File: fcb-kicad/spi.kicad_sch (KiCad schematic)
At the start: 0 parts

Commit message: hierarchic schemas, paljon muuta kivaa
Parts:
- added C10, C9: 100n, Capacitor_SMD:C_0603_1608Metric, symbol Device:C_Small
- added U3: DL-RTS4432, 000_sjt:DL-RTS4432_board, symbol 000_sjt:DL-RTS4432
- added U4, U7: LSM6DS3, Package_LGA:LGA-14_3x2.5mm_P0.5mm_LayoutBorder3x4y, symbol Sensor_Motion:LSM6DS3
- added U6: W25Q128JVS, Package_SO:SOIC-8_5.23x5.23mm_P1.27mm, symbol Memory_Flash:W25Q128JVS
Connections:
- new net: C10.1, U7.8 (VDD)
- new net: C9.1, U7.5 (VDDIO)
- new net +3V3: C10.2, C9.2
- new net GND: U7.2 (SDX), U7.3 (SCX), U7.6 (GND), U7.7 (GND)
- new net IMU_CS: U7.12 (CS)
- new net IMU_INT1: U7.4 (INT1)
- new net IMU_INT2: U7.9 (INT2)
- new net IMU_SDI: U7.14 (SDA)
- new net IMU_SDO: U7.1 (SDO/SA0)
- new net IMU_SPC: U7.13 (SCL)
- new net RAD_CS_N: U3.13 (nSEL)
- new net RAD_GPIO_0: U3.6 (GPIO_0)
- new net RAD_IRQ_N: U3.14 (nIRQ)
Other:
- note added: "CS: (1: SPI idle mode, 0: spi communication mode)"
- note added: "Datasheet has separate VDD and VDDIO VDDIO = Power supply for I/O pins Currently both connected to 3V3 VDD: 1.71-3.6 (V) VDDIO: 1.62-VDD + 0.1 (V)"
- note added: "IMU CIRCUIT"
- note added: "INT1: Programmable interrupt 1"
- note added: "SDI: SPI serial data input"
- note added: "SDO: SPI 4-wire interface serial data output"
- note added: "SDX and SCX can be alternatively connected to VDDIO"
- note added: "SPC: SPI serial port clock"
- company: (none) -> University of Oulu

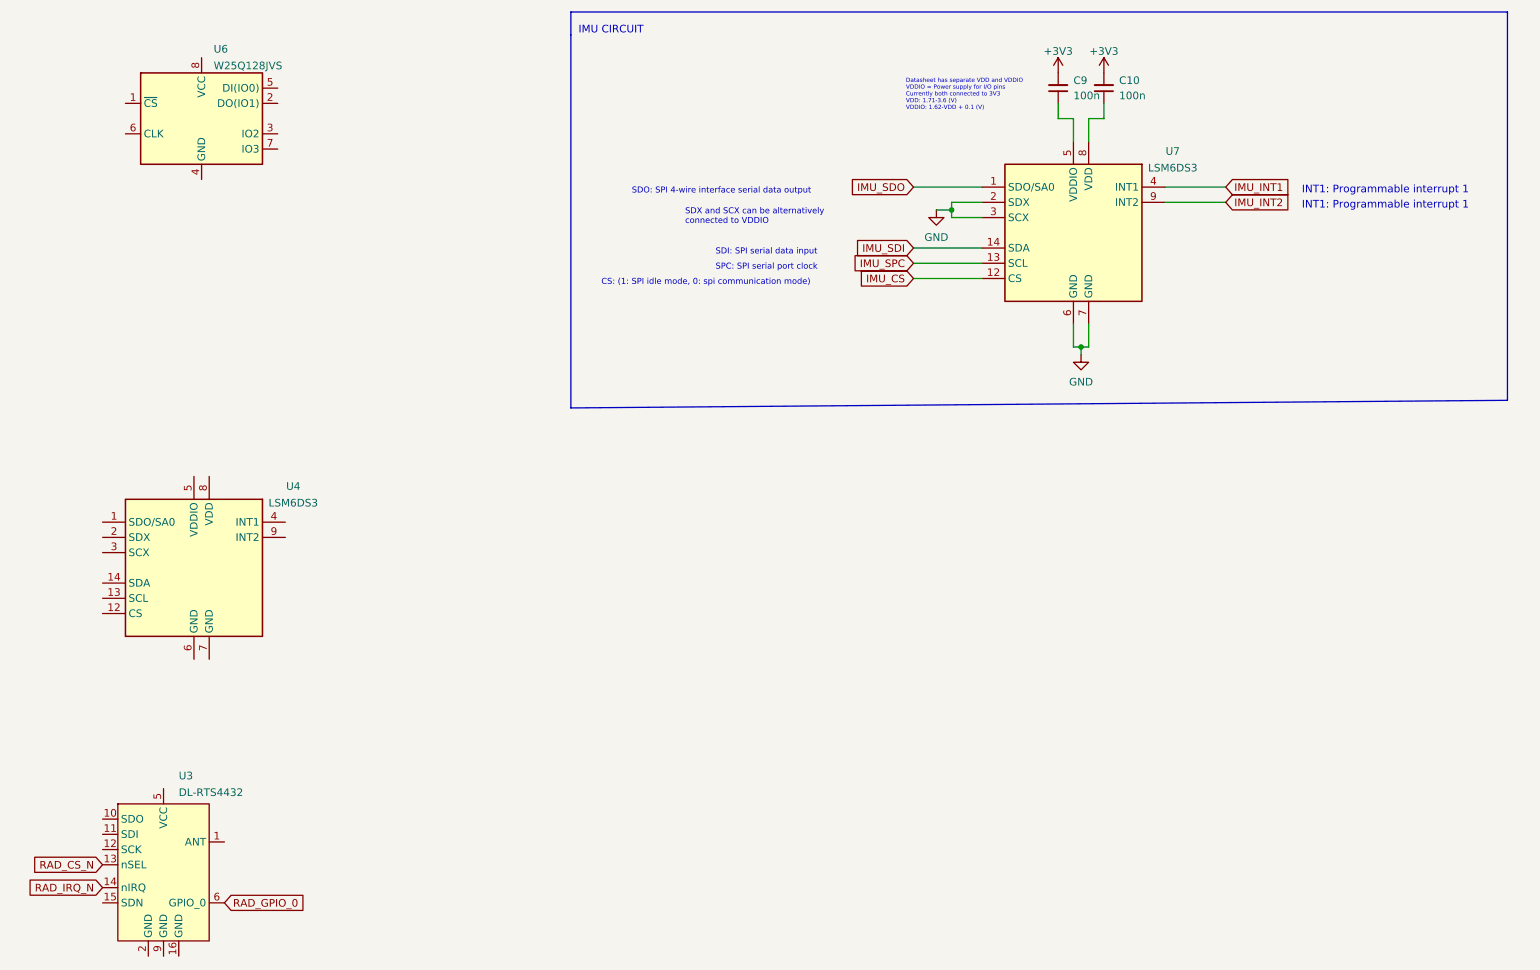
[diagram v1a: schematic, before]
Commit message: 4in1 connector library part, SPI CS pullups, migrate magnetometer cirtuit
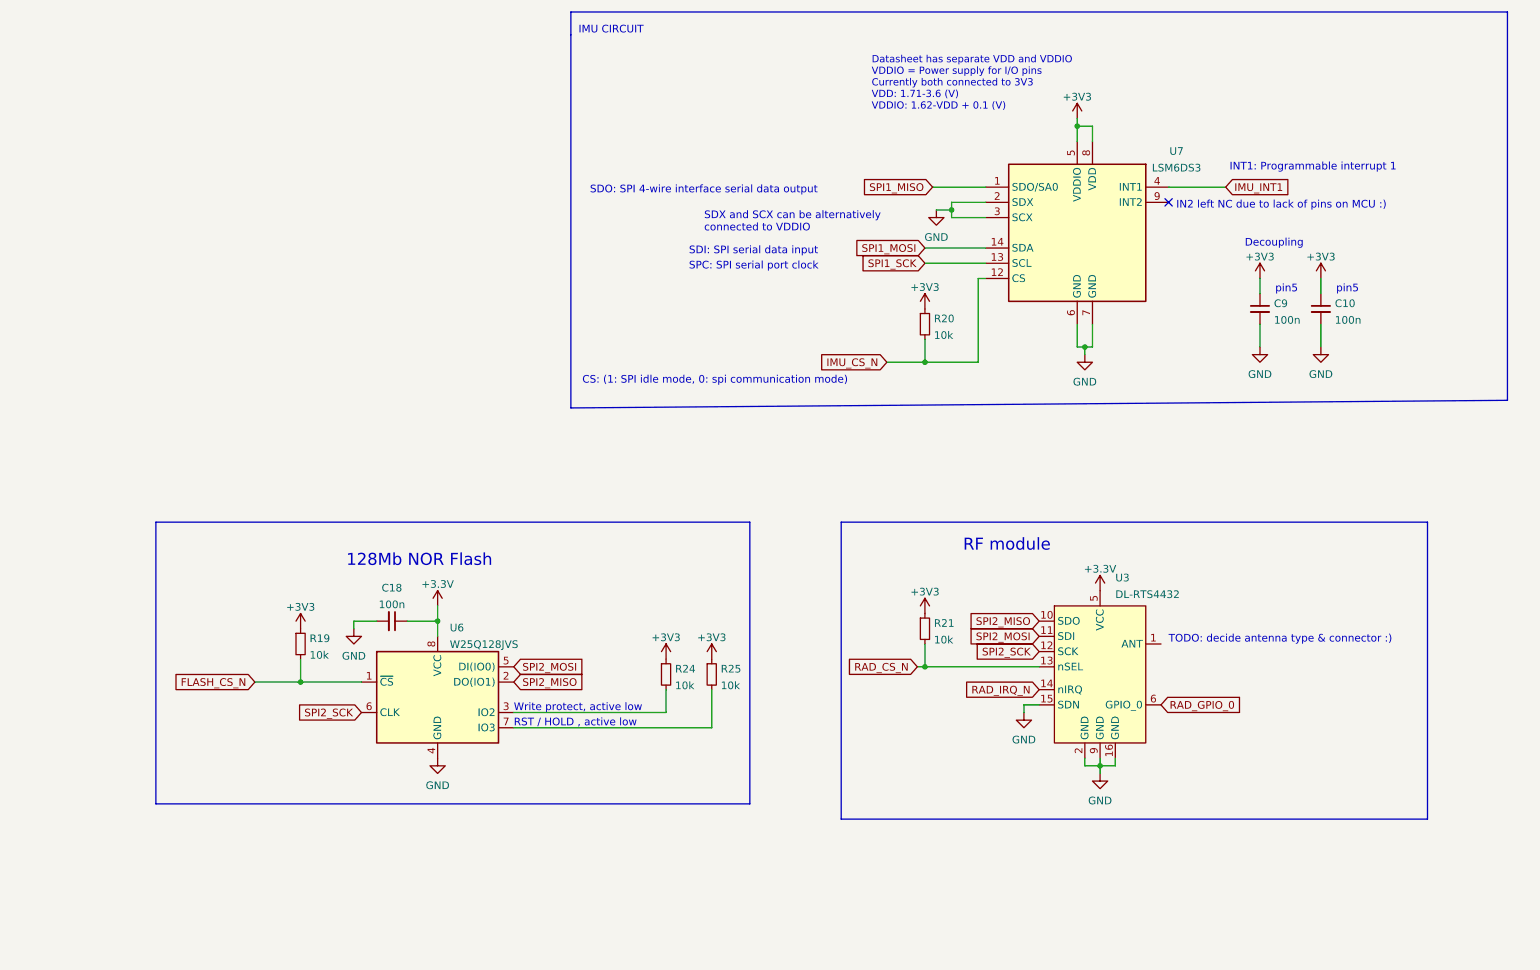
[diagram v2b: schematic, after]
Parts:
- removed U4: LSM6DS3, Package_LGA:LGA-14_3x2.5mm_P0.5mm_LayoutBorder3x4y, symbol Sensor_Motion:LSM6DS3
- added C18: 100n, Capacitor_SMD:C_0603_1608Metric, symbol Device:C_Small
- added R19, R20, R21, R24, R25: 10k, symbol Device:R_Small
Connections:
- net +3V3: now also C10.1, C9.1, U3.5 (VCC), U6.8 (VCC), U7.5 (VDDIO), U7.8 (VDD), C18.1, R19.1, R20.1, R21.1, R24.1, R25.1; no longer C10.2, C9.2
- net GND: now also C10.2, C9.2, U3.15 (SDN), U3.16 (GND), U3.2 (GND), U3.9 (GND), U6.4 (GND), C18.2
- net RAD_CS_N: now also R21.2
- net FLASH_CS_N: now reaches U6.1 (~{CS})
- net FLASH_CS_N: now also R19.2
- net SPI2_MISO: now reaches U6.2 (DO(IO1))
- net SPI2_MISO: now also U3.10 (SDO)
- net at U6.3 (IO2): now also R24.2
- net SPI2_MOSI: now reaches U6.5 (DI(IO0))
- net SPI2_MOSI: now also U3.11 (SDI)
- net SPI2_SCK: now reaches U6.6 (CLK)
- net SPI2_SCK: now also U3.12 (SCK)
- net at U6.7 (IO3): now also R25.2
- net IMU_CS renamed IMU_CS_N
- net IMU_CS_N: now also R20.2
- net IMU_INT2: no longer names the net of U7.9 (INT2)
- net IMU_SDI renamed SPI1_MOSI
- net IMU_SDO renamed SPI1_MISO
- net IMU_SPC renamed SPI1_SCK
- no-connect marks 0 -> 1
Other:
- note added: "128Mb NOR Flash"
- note added: "Decoupling"
- note added: "IN2 left NC due to lack of pins on MCU :)"
- note added: "RF module"
- note added: "RST / HOLD , active low"
- note added: "TODO: decide antenna type & connector :)"
- note added: "Write protect, active low"
- note added: "pin5"
- moved on the sheet: C10, C9, U3, U6, U7

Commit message: Schema rev0 done, Layout components grouped
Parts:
- added J10: Conn_Coaxial, 000_sjt:KH-IPEX-K501-29, symbol Connector:Conn_Coaxial
- R19, R20, R21, R24, R25: footprint (none) -> Resistor_SMD:R_0603_1608Metric
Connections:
- net GND: now also J10.2 (Ext)
- net ANT: now reaches U3.1 (ANT)
- net ANT: now also J10.1 (In)
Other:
- note added: "External antenna (IPEX) connector"
- note added: "VDD"
- note added: "VDDIO"
- note removed: "TODO: decide antenna type & connector :)"
- note removed: "pin5"
- title: (none) -> SPI peripherials
- moved on the sheet: C10, C9, R20, R21, U7

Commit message: PCB rev0: "Babby's first Leiska"
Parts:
- renumbered C18 to C14, C9 to C15, C10 to C16, J10 to J3, R19 to R16, R24 to R17, R25 to R18, R20 to R19, R21 to R20, U6 to U4, U7 to U5, U3 to U6
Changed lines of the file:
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@@
     (effects (font (size 1.2 1.2)) (justify left bottom))
   )
-  (text "VDD" (at 227.33 74.295 0)
-    (effects (font (size 1.27 1.27)) (justify left bottom))
+  (text "VDD" (at 227.33 74.295 180)
+    (effects (font (size 1.27 1.27)) (justify right bottom))
   )
   (text "RF module" (at 187.96 109.22 0)
@@
   (symbol (lib_id "Device:R_Small") (at 168.91 80.01 0) (unit 1)
     (in_bom yes) (on_board yes) (fields_autoplaced)
-    (property "Reference" "R20" (id 0) (at 170.4086 79.1015 0)
+    (property "Reference" "R19" (id 0) (at 170.4086 79.1015 0)
       (effects (font (size 1.27 1.27)) (justify left))
     )
@@
   (symbol (lib_id "Device:C_Small") (at 234.95 77.47 0) (unit 1)
     (in_bom yes) (on_board yes) (fields_autoplaced)
-    (property "Reference" "C10" (id 0) (at 237.2741 76.5678 0)
+    (property "Reference" "C16" (id 0) (at 237.2741 76.5678 0)
       (effects (font (size 1.27 1.27)) (justify left))
     )
@@
   (symbol (lib_id "power:+3V3") (at 194.31 45.72 0) (unit 1)
     (in_bom yes) (on_board yes)
-    (property "Reference" "#PWR046" (id 0) (at 194.31 49.53 0)
+    (property "Reference" "#PWR044" (id 0) (at 194.31 49.53 0)
       (effects (font (size 1.27 1.27)) hide)
     )
@@
   (symbol (lib_id "power:+3V3") (at 168.91 77.47 0) (unit 1)
     (in_bom yes) (on_board yes)
-    (property "Reference" "#PWR043" (id 0) (at 168.91 81.28 0)
+    (property "Reference" "#PWR041" (id 0) (at 168.91 81.28 0)
       (effects (font (size 1.27 1.27)) hide)
     )
@@
   (symbol (lib_id "Device:R_Small") (at 77.47 124.46 0) (unit 1)
     (in_bom yes) (on_board yes) (fields_autoplaced)
-    (property "Reference" "R19" (id 0) (at 78.9686 123.5515 0)
+    (property "Reference" "R16" (id 0) (at 78.9686 123.5515 0)
       (effects (font (size 1.27 1.27)) (justify left))
     )
@@
   (symbol (lib_id "power:GND") (at 234.95 83.82 0) (unit 1)
     (in_bom yes) (on_board yes) (fields_autoplaced)
-    (property "Reference" "#PWR050" (id 0) (at 234.95 90.17 0)
+    (property "Reference" "#PWR052" (id 0) (at 234.95 90.17 0)
       (effects (font (size 1.27 1.27)) hide)
     )
@@
   (symbol (lib_id "power:+3.3V") (at 100.33 118.11 0) (unit 1)
     (in_bom yes) (on_board yes) (fields_autoplaced)
-    (property "Reference" "#PWR040" (id 0) (at 100.33 121.92 0)
+    (property "Reference" "#PWR037" (id 0) (at 100.33 121.92 0)
       (effects (font (size 1.27 1.27)) hide)
     )
@@
   (symbol (lib_id "Device:R_Small") (at 175.26 121.92 0) (unit 1)
     (in_bom yes) (on_board yes) (fields_autoplaced)
-    (property "Reference" "R21" (id 0) (at 176.7586 121.0115 0)
+    (property "Reference" "R20" (id 0) (at 176.7586 121.0115 0)
       (effects (font (size 1.27 1.27)) (justify left))
     )
@@
   (symbol (lib_id "power:+3V3") (at 224.79 72.39 0) (unit 1)
     (in_bom yes) (on_board yes)
-    (property "Reference" "#PWR0117" (id 0) (at 224.79 76.2 0)
+    (property "Reference" "#PWR049" (id 0) (at 224.79 76.2 0)
       (effects (font (size 1.27 1.27)) hide)
     )
@@
   (symbol (lib_id "power:+3V3") (at 77.47 121.92 0) (unit 1)
     (in_bom yes) (on_board yes)
-    (property "Reference" "#PWR038" (id 0) (at 77.47 125.73 0)
+    (property "Reference" "#PWR035" (id 0) (at 77.47 125.73 0)
       (effects (font (size 1.27 1.27)) hide)
     )
@@
   (symbol (lib_id "power:+3V3") (at 138.43 127 0) (unit 1)
     (in_bom yes) (on_board yes)
-    (property "Reference" "#PWR0120" (id 0) (at 138.43 130.81 0)
+    (property "Reference" "#PWR039" (id 0) (at 138.43 130.81 0)
       (effects (font (size 1.27 1.27)) hide)
     )
@@
   (symbol (lib_id "Device:R_Small") (at 146.05 129.54 0) (unit 1)
     (in_bom yes) (on_board yes) (fields_autoplaced)
-    (property "Reference" "R25" (id 0) (at 147.5486 128.6315 0)
+    (property "Reference" "R18" (id 0) (at 147.5486 128.6315 0)
       (effects (font (size 1.27 1.27)) (justify left))
     )
@@
   (symbol (lib_id "power:GND") (at 224.79 83.82 0) (unit 1)
     (in_bom yes) (on_board yes) (fields_autoplaced)
-    (property "Reference" "#PWR049" (id 0) (at 224.79 90.17 0)
+    (property "Reference" "#PWR050" (id 0) (at 224.79 90.17 0)
       (effects (font (size 1.27 1.27)) hide)
     )
@@
   (symbol (lib_id "power:GND") (at 195.58 85.09 0) (unit 1)
     (in_bom yes) (on_board yes) (fields_autoplaced)
-    (property "Reference" "#PWR0115" (id 0) (at 195.58 91.44 0)
+    (property "Reference" "#PWR045" (id 0) (at 195.58 91.44 0)
       (effects (font (size 1.27 1.27)) hide)
     )
@@
   (symbol (lib_id "power:GND") (at 241.3 129.54 0) (unit 1)
     (in_bom yes) (on_board yes) (fields_autoplaced)
-    (property "Reference" "#PWR036" (id 0) (at 241.3 135.89 0)
+    (property "Reference" "#PWR053" (id 0) (at 241.3 135.89 0)
       (effects (font (size 1.27 1.27)) hide)
     )
@@
   (symbol (lib_id "Device:C_Small") (at 224.79 77.47 0) (unit 1)
     (in_bom yes) (on_board yes) (fields_autoplaced)
-    (property "Reference" "C9" (id 0) (at 227.1141 76.5678 0)
+    (property "Reference" "C15" (id 0) (at 227.1141 76.5678 0)
       (effects (font (size 1.27 1.27)) (justify left))
     )
@@
   (symbol (lib_id "power:+3V3") (at 175.26 119.38 0) (unit 1)
     (in_bom yes) (on_board yes)
-    (property "Reference" "#PWR044" (id 0) (at 175.26 123.19 0)
+    (property "Reference" "#PWR043" (id 0) (at 175.26 123.19 0)
       (effects (font (size 1.27 1.27)) hide)
     )
@@
   (symbol (lib_id "power:+3V3") (at 234.95 72.39 0) (unit 1)
     (in_bom yes) (on_board yes)
-    (property "Reference" "#PWR0116" (id 0) (at 234.95 76.2 0)
+    (property "Reference" "#PWR051" (id 0) (at 234.95 76.2 0)
       (effects (font (size 1.27 1.27)) hide)
     )
@@
   (symbol (lib_id "Memory_Flash:W25Q128JVS") (at 100.33 133.35 0) (unit 1)
     (in_bom yes) (on_board yes) (fields_autoplaced)
-    (property "Reference" "U6" (id 0) (at 102.3494 121.7635 0)
+    (property "Reference" "U4" (id 0) (at 102.3494 121.7635 0)
       (effects (font (size 1.27 1.27)) (justify left))
     )
@@
   (symbol (lib_id "Device:C_Small") (at 92.71 120.65 270) (unit 1)
     (in_bom yes) (on_board yes) (fields_autoplaced)
-    (property "Reference" "C18" (id 0) (at 92.7036 115.1214 90))
+    (property "Reference" "C14" (id 0) (at 92.7036 115.1214 90))
     (property "Value" "100n" (id 1) (at 92.7036 117.8965 90))
     (property "Footprint" "Capacitor_SMD:C_0603_1608Metric" (id 2) (at 92.71 120.65 0)
@@
   (symbol (lib_id "Device:R_Small") (at 138.43 129.54 0) (unit 1)
     (in_bom yes) (on_board yes) (fields_autoplaced)
-    (property "Reference" "R24" (id 0) (at 139.9286 128.6315 0)
+    (property "Reference" "R17" (id 0) (at 139.9286 128.6315 0)
       (effects (font (size 1.27 1.27)) (justify left))
     )
@@
   (symbol (lib_id "power:GND") (at 86.36 121.92 0) (unit 1)
     (in_bom yes) (on_board yes) (fields_autoplaced)
-    (property "Reference" "#PWR039" (id 0) (at 86.36 128.27 0)
+    (property "Reference" "#PWR036" (id 0) (at 86.36 128.27 0)
       (effects (font (size 1.27 1.27)) hide)
     )
@@
   (symbol (lib_id "power:GND") (at 100.33 143.51 0) (unit 1)
     (in_bom yes) (on_board yes) (fields_autoplaced)
-    (property "Reference" "#PWR041" (id 0) (at 100.33 149.86 0)
+    (property "Reference" "#PWR038" (id 0) (at 100.33 149.86 0)
       (effects (font (size 1.27 1.27)) hide)
     )
@@
   (symbol (lib_id "Sensor_Motion:LSM6DS3") (at 194.31 64.77 0) (unit 1)
     (in_bom yes) (on_board yes)
-    (property "Reference" "U7" (id 0) (at 210.8752 51.1767 0))
+    (property "Reference" "U5" (id 0) (at 210.8752 51.1767 0))
     (property "Value" "LSM6DS3" (id 1) (at 210.8752 53.9518 0))
     (property "Footprint" "Package_LGA:LGA-14_3x2.5mm_P0.5mm_LayoutBorder3x4y" (id 2) (at 184.15 82.55 0)
@@
   (symbol (lib_id "000_sjt:DL-RTS4432") (at 210.82 124.46 0) (unit 1)
     (in_bom yes) (on_board yes)
-    (property "Reference" "U3" (id 0) (at 213.36 113.4299 0)
+    (property "Reference" "U6" (id 0) (at 213.36 113.4299 0)
       (effects (font (size 1.27 1.27)) (justify left))
     )
@@
   (symbol (lib_id "power:GND") (at 171.45 60.96 0) (unit 1)
     (in_bom yes) (on_board yes) (fields_autoplaced)
-    (property "Reference" "#PWR0118" (id 0) (at 171.45 67.31 0)
+    (property "Reference" "#PWR042" (id 0) (at 171.45 67.31 0)
       (effects (font (size 1.27 1.27)) hide)
     )
@@
   (symbol (lib_id "power:GND") (at 198.12 135.89 0) (unit 1)
     (in_bom yes) (on_board yes) (fields_autoplaced)
-    (property "Reference" "#PWR045" (id 0) (at 198.12 142.24 0)
+    (property "Reference" "#PWR046" (id 0) (at 198.12 142.24 0)
       (effects (font (size 1.27 1.27)) hide)
     )
@@
   (symbol (lib_id "Connector:Conn_Coaxial") (at 241.3 124.46 0) (unit 1)
     (in_bom yes) (on_board yes) (fields_autoplaced)
-    (property "Reference" "J10" (id 0) (at 243.84 123.8447 0)
+    (property "Reference" "J3" (id 0) (at 243.84 123.8447 0)
       (effects (font (size 1.27 1.27)) (justify left))
     )
@@
   (symbol (lib_id "power:+3V3") (at 146.05 127 0) (unit 1)
     (in_bom yes) (on_board yes)
-    (property "Reference" "#PWR0119" (id 0) (at 146.05 130.81 0)
-      (effects (font (size 1.27 1.27)) hide)
-    )
+    (property "Reference" "#PWR040" (id 0) (at 146.05 130.81 0)
+      (effects (font (size 1.27 1.27)) hide)
+    )
